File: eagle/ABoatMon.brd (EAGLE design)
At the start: 86.4 x 61 mm, 33 parts, among them J1 VUSB, J2 GND, J3 GND, J4 LIPO, J5 U.FL, X1 MKDSN1,5/2-5,08

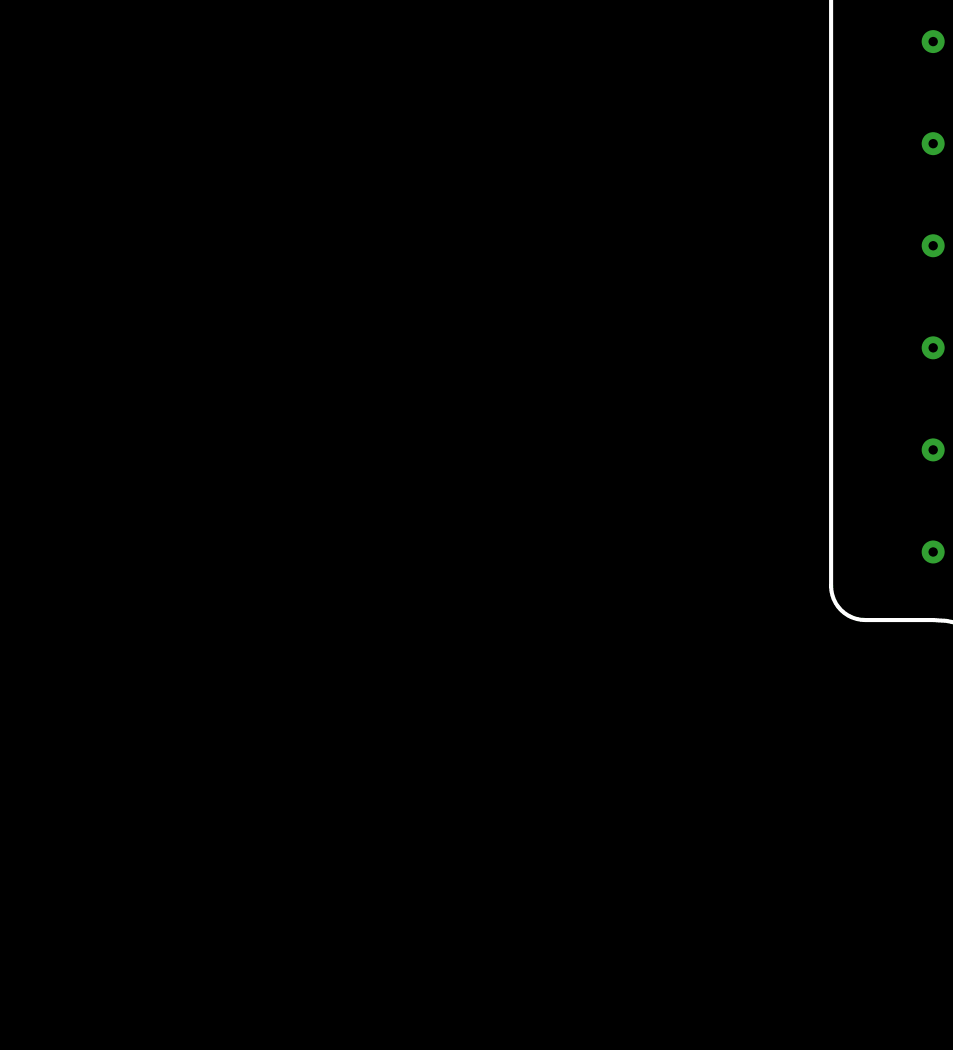
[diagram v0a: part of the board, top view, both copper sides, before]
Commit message: Started R0.9 1. Mounting hole wrong place 2. Regulator board needs to move down due to overlapping edge of casterlated holes 3. Mobile module needs to move right 1mm due to sharp lower left edge hitting box 4. Need to move Ufl connector left due to grommets in box 5. Can make the edge tabs slightly deeper, will help routing 6. Need to add lipo connector and route to VUSB 7. Need to move Capacitor below regulator board
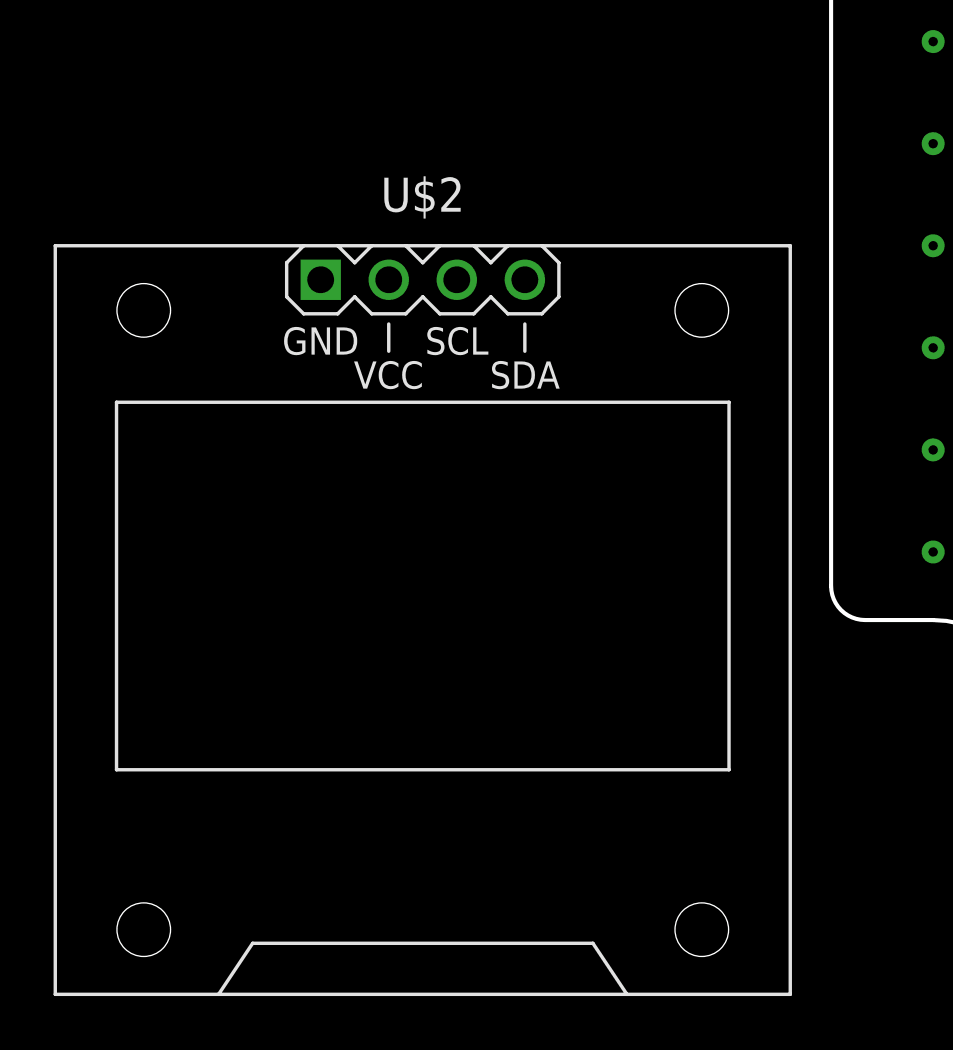
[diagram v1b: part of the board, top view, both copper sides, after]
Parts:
- added U$2: DISPLAY-OLED-128X64-I2C, diy-modules:DISPLAY-OLED-128X64-I2C
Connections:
- net GND: now also U$2.1
- net VCC: now also U$2.2
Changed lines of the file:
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@@
 <attribute name="VALUE" x="34.29" y="50.038" size="0.6096" layer="27" font="vector" ratio="20"/>
+</element>
+<element name="U$2" library="diy-modules" package="DISPLAY-OLED-128X64-I2C" value="DISPLAY-OLED-128X64-I2C" x="-13.97" y="12.7" smashed="yes">
+<attribute name="NAME" x="-13.97" y="27.94" size="1.27" layer="25" align="bottom-center"/>
+<attribute name="VALUE" x="-13.97" y="-2.54" size="1.27" layer="27" align="top-center"/>
 </element>
 </elements>
@@
 <via x="49.53" y="17.78" extent="1-16" drill="0.35"/>
 <via x="48.26" y="10.16" extent="1-16" drill="0.35"/>
+<contactref element="U$2" pad="1"/>
+<wire x1="5.08" y1="26.67" x2="-17.78" y2="25.4" width="0" layer="19" extent="1-1"/>
 </signal>
 <signal name="VUSB" class="1">
@@
 <wire x1="10.0965" y1="38.1" x2="10.16" y2="38.1" width="0.6096" layer="1"/>
 <wire x1="5.1435" y1="45.72" x2="5.105" y2="45.7411" width="0.6096" layer="1"/>
+<contactref element="U$2" pad="2"/>
+<wire x1="-15.24" y1="25.4" x2="7.8105" y2="41.148" width="0" layer="19" extent="1-1"/>
 </signal>
 <signal name="D5_LED_SWITCH">

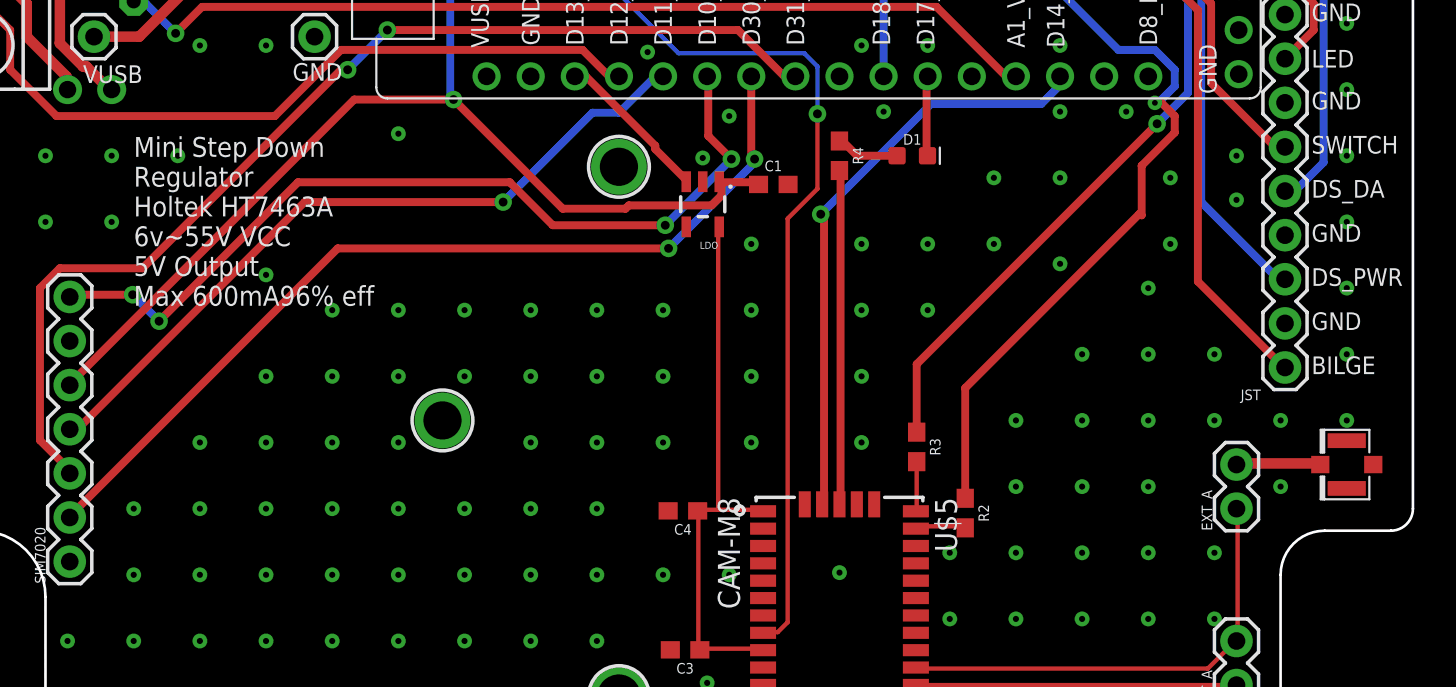
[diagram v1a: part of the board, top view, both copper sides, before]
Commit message: Mounting hole and ufl moved
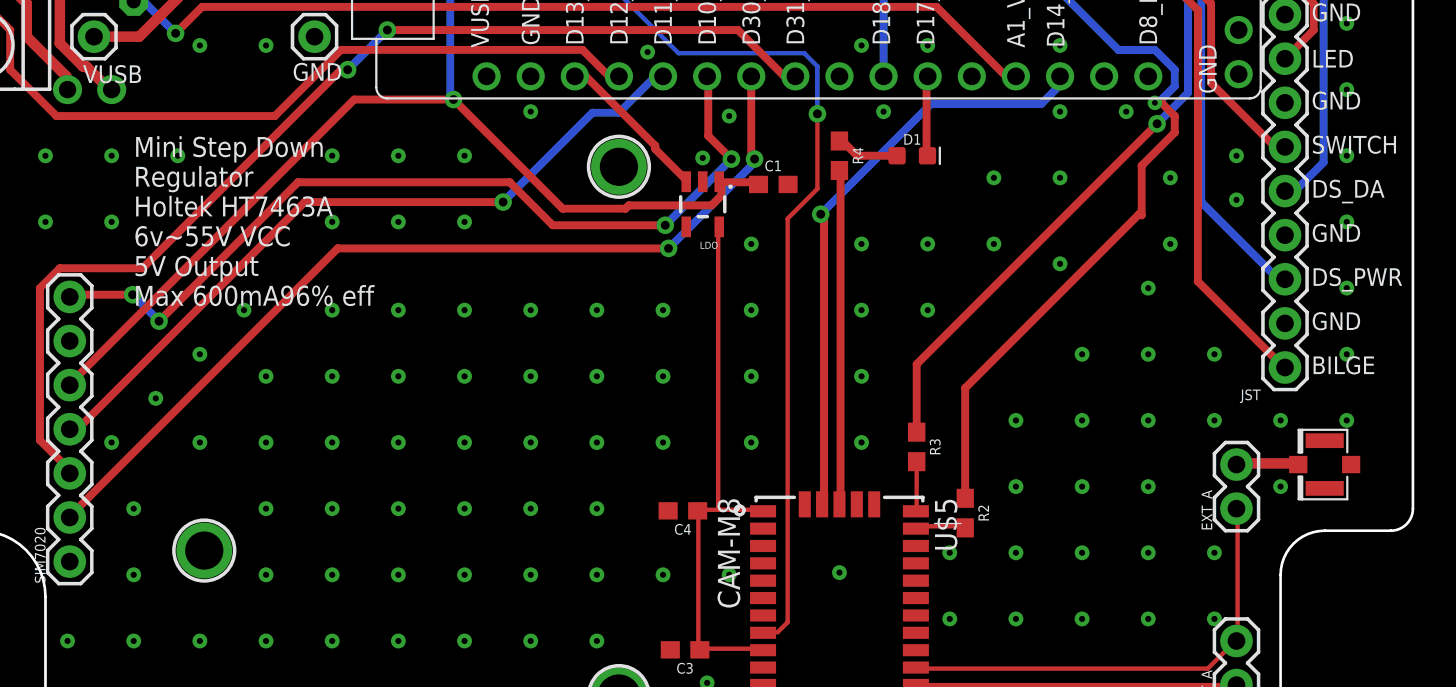
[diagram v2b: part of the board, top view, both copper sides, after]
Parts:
- moved U$9 15.6 mm to (18.0, 11.6)
- moved J5 1.27 mm to (82.5, 16.5)
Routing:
- net N$6: track 4.86 -> 3.59 mm
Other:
- board text added: "v0.9 gregcope@gmail.com Moteino M0 ABoatMon Shield"
- board text removed: "v0.899 gregcope@gmail.com Moteino M0 ABoatMon Shield"
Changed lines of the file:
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@@
 <?xml version="1.0" encoding="utf-8"?>
 <!DOCTYPE eagle SYSTEM "eagle.dtd">
-<eagle version="9.4.2">
+<eagle version="9.5.2">
 <drawing>
 <settings>
@@
 <dimension x1="11.684" y1="41.148" x2="24.384" y2="41.148" x3="18.034" y3="39.878" textsize="1.778" layer="25"/>
 <dimension x1="11.684" y1="41.148" x2="11.684" y2="58.928" x3="27.305" y3="50.038" textsize="1.778" layer="25"/>
-<text x="51.181" y="20.447" size="1.778" layer="26">v0.899
+<text x="51.181" y="20.447" size="1.778" layer="26">v0.9
 gregcope@gmail.com
 Moteino M0
@@
 </element>
 <element name="U$3" library="microbuilder" package="MOUNTINGHOLE_2.0_PLATED" value="MOUNTINGHOLE2.0" x="41.91" y="33.655" smashed="yes"/>
-<element name="U$9" library="microbuilder" package="MOUNTINGHOLE_2.0_PLATED" value="MOUNTINGHOLE2.0" x="31.75" y="19.05" smashed="yes"/>
-<element name="J5" library="SparkFun-Connectors" library_urn="urn:adsk.eagle:library:513" package="U.FL" package3d_urn="urn:adsk.eagle:package:38237/1" value="U.FL" x="83.82" y="16.51" smashed="yes" rot="R180">
-<attribute name="PROD_ID" value="CONN-09193" x="83.82" y="16.51" size="1.778" layer="27" rot="R180" display="off"/>
-<attribute name="SF_ID" value="WRL-09144" x="83.82" y="16.51" size="1.778" layer="27" rot="R180" display="off"/>
-<attribute name="VALUE" x="83.82" y="19.05" size="0.6096" layer="27" font="vector" ratio="20" rot="R180" align="top-left"/>
+<element name="U$9" library="microbuilder" package="MOUNTINGHOLE_2.0_PLATED" value="MOUNTINGHOLE2.0" x="18.034" y="11.557" smashed="yes"/>
+<element name="J5" library="SparkFun-Connectors" library_urn="urn:adsk.eagle:library:513" package="U.FL" package3d_urn="urn:adsk.eagle:package:38237/1" value="U.FL" x="82.55" y="16.51" smashed="yes" rot="R180">
+<attribute name="PROD_ID" value="CONN-09193" x="82.55" y="16.51" size="1.778" layer="27" rot="R180" display="off"/>
+<attribute name="SF_ID" value="WRL-09144" x="82.55" y="16.51" size="1.778" layer="27" rot="R180" display="off"/>
+<attribute name="VALUE" x="82.55" y="19.05" size="0.6096" layer="27" font="vector" ratio="20" rot="R180" align="top-left"/>
 </element>
 <element name="INT_A" library="SparkFun-Connectors" library_urn="urn:adsk.eagle:library:513" package="1X02" package3d_urn="urn:adsk.eagle:package:38039/1" value="" x="77.47" y="3.81" smashed="yes" rot="R90">
@@
 <via x="21.59" y="10.16" extent="1-16" drill="0.35"/>
 <via x="13.97" y="10.16" extent="1-16" drill="0.35"/>
-<via x="17.78" y="10.16" extent="1-16" drill="0.35"/>
+<via x="33.02" y="17.78" extent="1-16" drill="0.35"/>
 <via x="13.97" y="6.35" extent="1-16" drill="0.35"/>
 <via x="10.16" y="6.35" extent="1-16" drill="0.35"/>
@@
 <via x="5.08" y="38.1" extent="1-16" drill="0.35"/>
 <via x="13.97" y="13.97" extent="1-16" drill="0.35"/>
-<via x="17.78" y="13.97" extent="1-16" drill="0.35"/>
+<via x="29.21" y="30.48" extent="1-16" drill="0.35"/>
 <via x="21.59" y="13.97" extent="1-16" drill="0.35"/>
 <via x="21.59" y="17.78" extent="1-16" drill="0.35"/>
@@
 <via x="25.4" y="17.78" extent="1-16" drill="0.35"/>
 <via x="25.4" y="13.97" extent="1-16" drill="0.35"/>
-<via x="21.59" y="27.432" extent="1-16" drill="0.35"/>
 <via x="25.4" y="25.4" extent="1-16" drill="0.35"/>
-<via x="29.21" y="35.56" extent="1-16" drill="0.35"/>
 <via x="29.21" y="13.97" extent="1-16" drill="0.35"/>
 <via x="29.21" y="17.78" extent="1-16" drill="0.35"/>
@@
 <via x="48.26" y="10.16" extent="1-16" drill="0.35"/>
 <contactref element="U$2" pad="1"/>
+<via x="20.32" y="25.4" extent="1-16" drill="0.35"/>
+<via x="17.78" y="22.86" extent="1-16" drill="0.35"/>
+<via x="15.24" y="20.32" extent="1-16" drill="0.35"/>
+<via x="12.7" y="17.78" extent="1-16" drill="0.35"/>
+<via x="25.4" y="30.48" extent="1-16" drill="0.35"/>
+<via x="33.02" y="30.48" extent="1-16" drill="0.35"/>
+<via x="29.21" y="34.29" extent="1-16" drill="0.35"/>
+<via x="33.02" y="34.29" extent="1-16" drill="0.35"/>
+<via x="25.4" y="34.29" extent="1-16" drill="0.35"/>
+<via x="36.83" y="36.83" extent="1-16" drill="0.35"/>
 <wire x1="5.08" y1="26.67" x2="-17.78" y2="25.4" width="0" layer="19" extent="1-1"/>
 </signal>
@@
 <wire x1="5.1435" y1="45.72" x2="5.105" y2="45.7411" width="0.6096" layer="1"/>
 <contactref element="U$2" pad="2"/>
-<wire x1="-15.24" y1="25.4" x2="7.8105" y2="41.148" width="0" layer="19" extent="1-1"/>
+<wire x1="-15.24" y1="25.4" x2="10.16" y2="38.1" width="0" layer="19" extent="1-1"/>
 </signal>
 <signal name="D5_LED_SWITCH">
@@
 <contactref element="J5" pad="FEED"/>
 <contactref element="EXT_A" pad="2"/>
-<wire x1="77.5335" y1="16.5735" x2="82.1055" y2="16.5735" width="0.6096" layer="1"/>
-<wire x1="82.1055" y1="16.5735" x2="82.295" y2="16.51" width="0.6096" layer="1"/>
+<wire x1="77.5335" y1="16.5735" x2="80.8355" y2="16.5735" width="0.6096" layer="1"/>
+<wire x1="80.8355" y1="16.5735" x2="81.025" y2="16.51" width="0.6096" layer="1"/>
 <wire x1="77.5335" y1="16.5735" x2="77.47" y2="16.51" width="0.6096" layer="1"/>
 </signal>

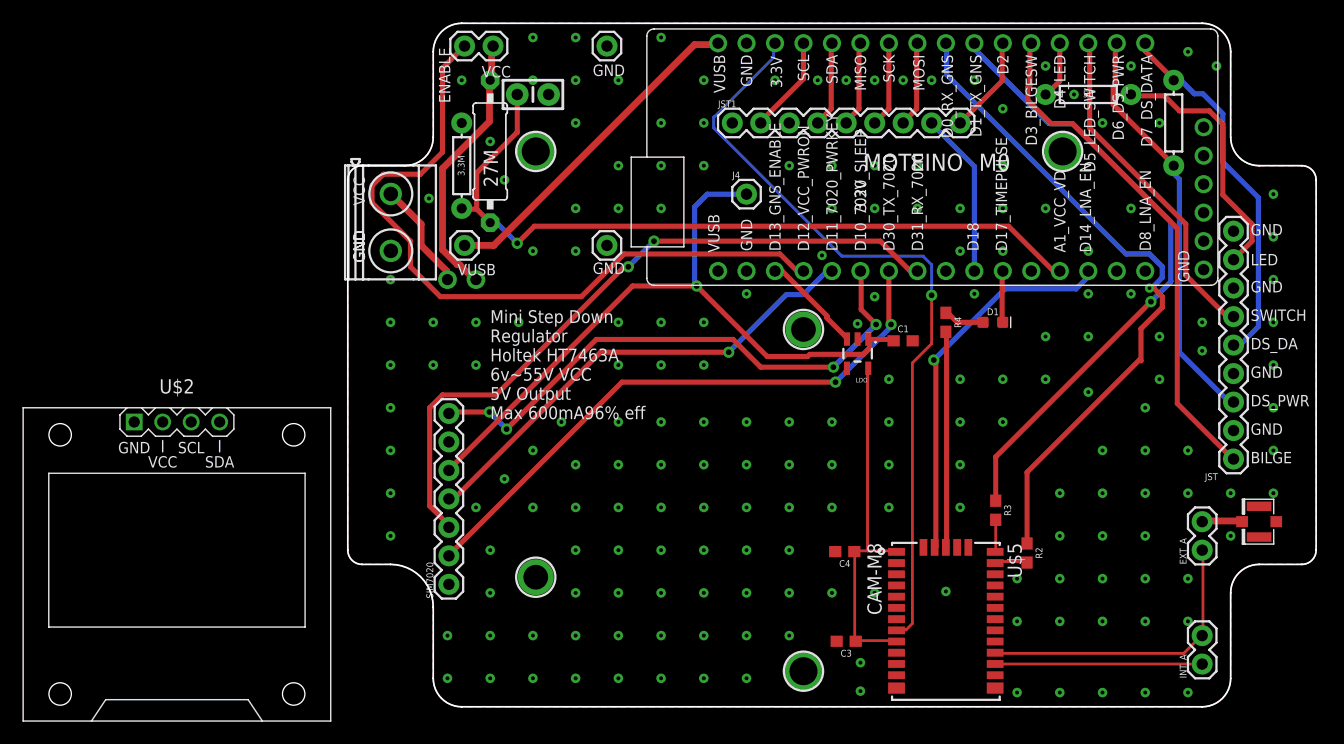
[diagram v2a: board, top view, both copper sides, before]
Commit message: pushed out tab sizes on either end
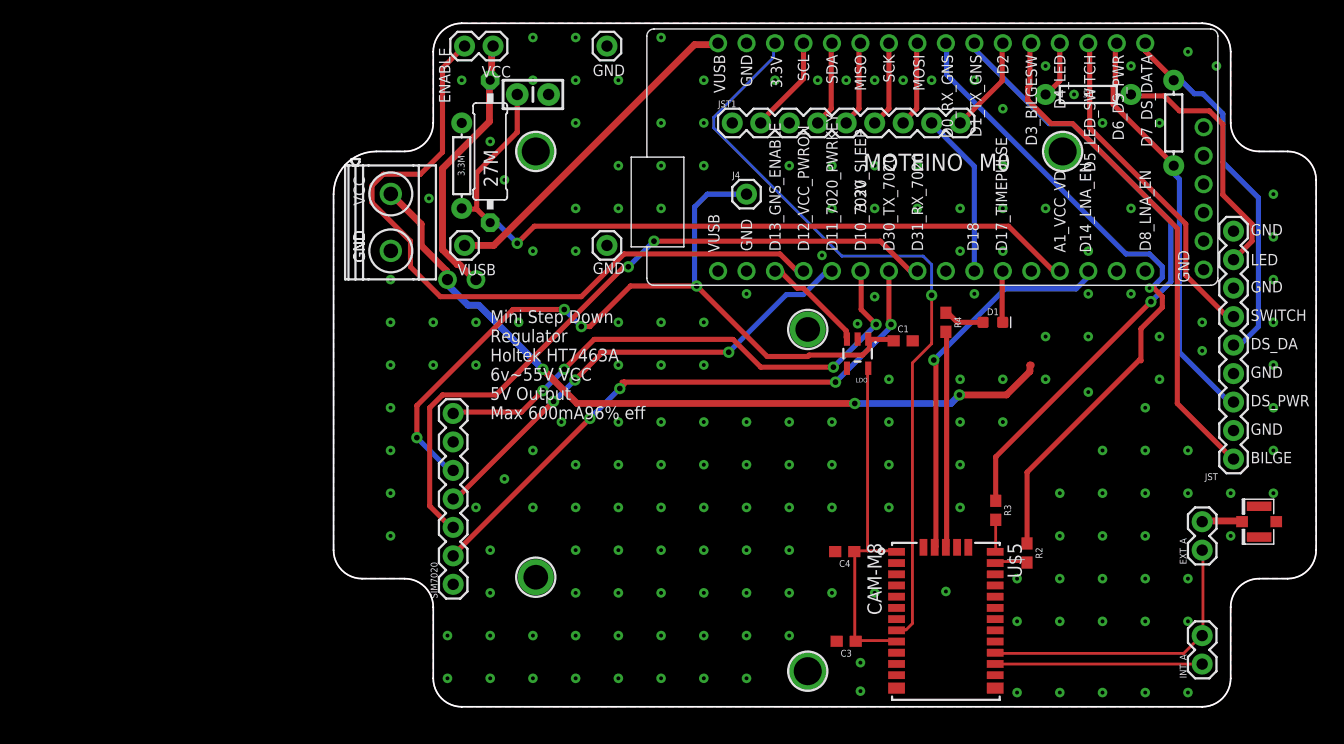
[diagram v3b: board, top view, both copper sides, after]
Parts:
- removed U$2: DISPLAY-OLED-128X64-I2C, diy-modules:DISPLAY-OLED-128X64-I2C
- moved U$1 0.38 mm to (42.3, 3.17)
- moved U$3 0.38 mm to (42.3, 33.7)
- moved SIM7020 0.38 mm to (10.7, 10.9)
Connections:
- net GND: no longer U$2.1
- net VCC: no longer U$2.2
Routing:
- net VCC: track 9.78 -> 68.5 mm, vias 0 -> 3
- net LIPO: track 62.8 -> 71.9 mm, vias 1 -> 4
- net D10_7020_SLEEP: track 50.2 -> 48.5 mm
- net D13_GNS_ENABLE: track 9.08 -> 9.89 mm
- net D11_7020_PWRKEY: track 43.4 -> 43.1 mm, vias 1 -> 3
- net D30_TX_7020: track 53.0 -> 52.9 mm, vias 2 -> 4
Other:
- board size 86.4 x 61 mm -> 87.6 x 61 mm
